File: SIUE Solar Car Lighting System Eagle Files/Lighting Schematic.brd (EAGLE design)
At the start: 68.2 x 77.5 mm, 43 parts, among them IC1 74HC08N, IC2 74HC08N, IC3 74LS04N, IC4 NE555N, Q1 RFP30N06LE, Q2 RFP30N06LE, Q3 RFP30N06LE, Q4 RFP30N06LE, Q5 RFP30N06LE, Q6 RFP30N06LE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

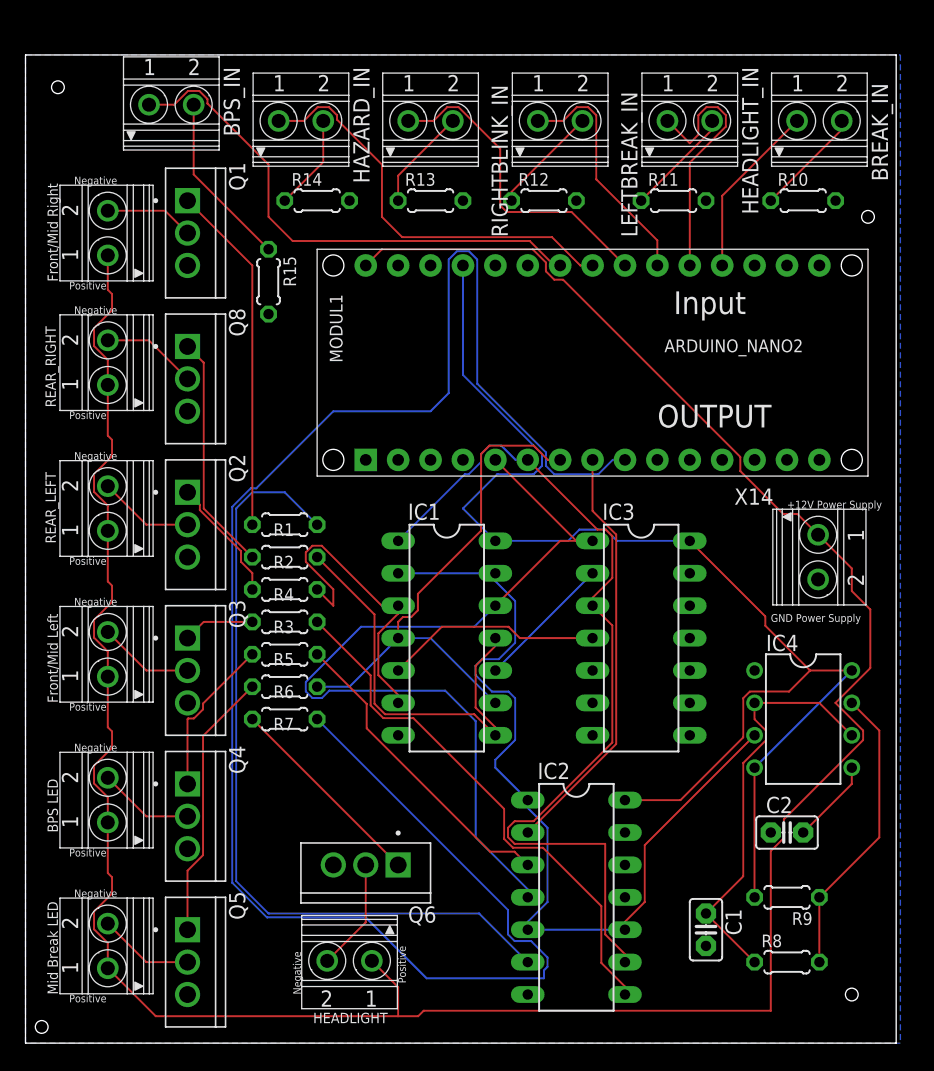
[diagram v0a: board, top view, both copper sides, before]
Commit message: Add files via upload
Several changes made in this version:
- For the input connections I created an on-board 5V source on the positive end of the Input connector, and then a 10k pull-down resistor connected to the arduino on the other. This should make sure that the arduino isn't reading any floating signals when the switch is open and the 5V can not flow through the switch. The 5V source on the pins will also eliminate the need for an external power supply running across the switches. 
- This 5V source is included on the BPS_IN connector to allow for testing, in practical use since the BMS will be sending an HIGH Output when functioning correctly and go LOW when error is detected we should only need to plug in to the BPS IN-2 pin which has the pull-down resistor connected to it.
- I found that I was flawed in thinking I could set two logic gates entering the same node, which likely resulted in the issues I found when I first made the PCB board and will now be corrected with the addition of a single 74HC32 Quad 2-input OR chip. The new EAGLE Files and the LTSpice files reflect this change.
- I found that the holes I had originally placed where too small so I changed from 4 of those tiny holes to 3 - 3.2mm mounting holes placed at roughly 3 corners of the PCB to allow for mounting. 
-Minor movements in the EAGLE schematic or Board files to allow for easier soldering and less crowding.
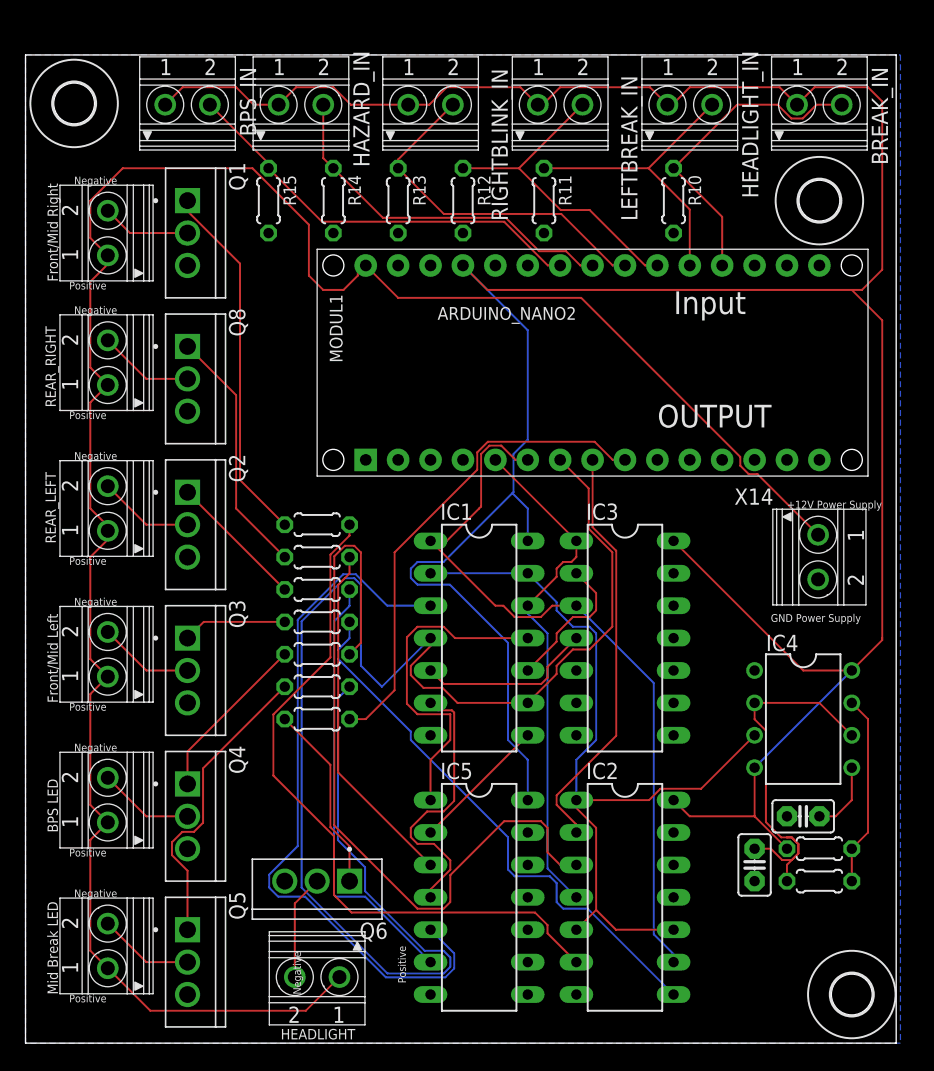
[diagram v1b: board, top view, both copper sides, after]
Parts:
- added IC5: 74HC32N, 74xx-eu:DIL14
- added U$1, U$2, U$3: (no value), holes:3,2
- moved R10 10.2 mm to (50.8, 66.0), turned to 270 degrees
- moved R11 10.2 mm to (40.6, 66.0), turned to 270 degrees
- moved R8 6.84 mm to (62.2, 12.7)
- moved R15 6.35 mm to (19.1, 66.0)
- moved R12 6.35 mm to (34.3, 66.0), turned to 270 degrees
- moved C1 6.35 mm to (57.1, 14.0)
- moved R9 4.58 mm to (62.2, 15.2)
- moved Q6 4.02 mm to (22.9, 12.7)
- moved IC2 3.81 mm to (47.0, 11.4)
- moved HEADLIGHT 2.84 mm to (22.9, 5.08)
- moved IC1 2.54 mm to (35.6, 31.8)
- moved R1 2.54 mm to (22.9, 40.6)
- moved R13 2.54 mm to (29.2, 66.0), turned to 270 degrees
- moved R2 2.54 mm to (22.9, 38.1)
- moved R3 2.54 mm to (22.9, 33.0)
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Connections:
- removed net LEFTBLINKCLK: IC1.3, IC1.6, R4.1
- removed net N$46: BREAK_IN.2, R10.1
- removed net N$48: HEADLIGHT_IN.2, R11.1
- removed net N$50: LEFTBREAK_IN.2, R12.1
- removed net N$54: R13.1, RIGHTBLINK_IN.2
- removed net N$56: HAZARD_IN.2, R14.1
- removed net N$58: BPS_IN.2, R15.1
- removed net RIGHTBLINKCLK: IC1.11, IC1.8, R2.1
- new net N$17: IC5.3, R2.1
- new net N$18: IC1.8, IC5.2
- new net N$19: IC1.11, IC5.1
- new net N$20: IC5.6, R4.1
- new net N$21: IC1.6, IC5.4
- new net N$22: IC1.3, IC5.5
- net BPS_IN: now also BPS_IN.2, R15.1; no longer BPS_IN.1
- net BREAK_IN: now also BREAK_IN.2, R10.1; no longer BREAK_IN.1
- net GND: now also IC5.7
- net HAZARD_IN: now also HAZARD_IN.2, R14.1; no longer HAZARD_IN.1
- net HEADLIGHT_IN: now also HEADLIGHT_IN.2, R11.1; no longer HEADLIGHT_IN.1
- net LEFTBLINK_IN: now also LEFTBREAK_IN.2, R12.1; no longer LEFTBREAK_IN.1
- net RIGHTBLINK_IN: now also R13.1, RIGHTBLINK_IN.2; no longer RIGHTBLINK_IN.1
- net VCC: now also BPS_IN.1, BREAK_IN.1, HAZARD_IN.1, HEADLIGHT_IN.1, IC5.14, LEFTBREAK_IN.1, RIGHTBLINK_IN.1
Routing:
- net VCC: track 104.2 -> 244.0 mm
- net HEADLIGHT: track 144.9 -> 38.3 mm
- net BREAK: track 42.1 -> 120.6 mm
- net N$22: track 0.00 -> 56.3 mm
- net +12V: track 211.0 -> 161.9 mm
- net N$10: track 24.5 -> 60.4 mm
- net N$20: track 0.00 -> 34.2 mm
- net RIGHTBLINKCLK: track 32.8 -> 0.00 mm
- net RIGHTBLINK: track 68.3 -> 40.5 mm
- net N$17: track 0.00 -> 27.5 mm
- net N$19: track 0.00 -> 26.5 mm
- net LEFTBLINKCLK: track 25.2 -> 0.00 mm
- net N$21: track 0.00 -> 21.5 mm
- net N$58: track 13.8 -> 0.00 mm
- net BREAK_IN: track 13.8 -> 25.3 mm
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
